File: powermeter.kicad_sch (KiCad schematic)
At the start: 21 parts, among them J1 Conn_01x04, J2 Conn_01x07, J3 Conn_01x07, Q1 S8550, U1 XIAO BLE, U2 HX711, U3 MPU-6050

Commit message: Fix 5v-GND short. Minor tweaks on layout
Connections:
- net GND: no longer J3.7 (Pin_7), U1.14 (5v)
- new net 5V: J3.7 (Pin_7), U1.14 (5v)

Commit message: Fix AD0 MPU6050 to GND
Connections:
- net GND: now also U3.9 (AD0)
- no-connect marks 6 -> 5
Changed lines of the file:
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@@
   (no_connect (at 88.9 91.44))
   (no_connect (at 220.98 59.69))
-  (no_connect (at 88.9 81.28))
   (no_connect (at 124.46 83.82))
   (wire (pts (xy 72.39 30.48) (xy 87.63 30.48))
@@
   )
   (wire (pts (xy 157.48 62.23) (xy 157.48 69.85))
+    (stroke (width 0) (type default))
+  )
+  (wire (pts (xy 86.36 81.28) (xy 88.9 81.28))
     (stroke (width 0) (type default))
   )
@@
         )
       )
+    )
+  )
+  (symbol (lib_id "power:GND") (at 86.36 81.28 270) (mirror x) (unit 1)
+    (in_bom yes) (on_board yes) (dnp no) (fields_autoplaced)
+    (property "Reference" "#PWR019" (at 80.01 81.28 0)
+      (effects (font (size 1.27 1.27)) hide)
+    )
+    (property "Value" "GND" (at 82.55 81.28 90)
+      (effects (font (size 1.27 1.27)) (justify right))
+    )
+    (property "Footprint" "" (at 86.36 81.28 0)
+      (effects (font (size 1.27 1.27)) hide)
+    )
+    (property "Datasheet" "" (at 86.36 81.28 0)
+      (effects (font (size 1.27 1.27)) hide)
+    )
+    (pin "1")
+    (instances
+      (project "powermeter"
+        (path "/59c6f472-5476-453e-ab78-e7815b2e4e17"
+          (reference "#PWR019") (unit 1)
+        )
+      )

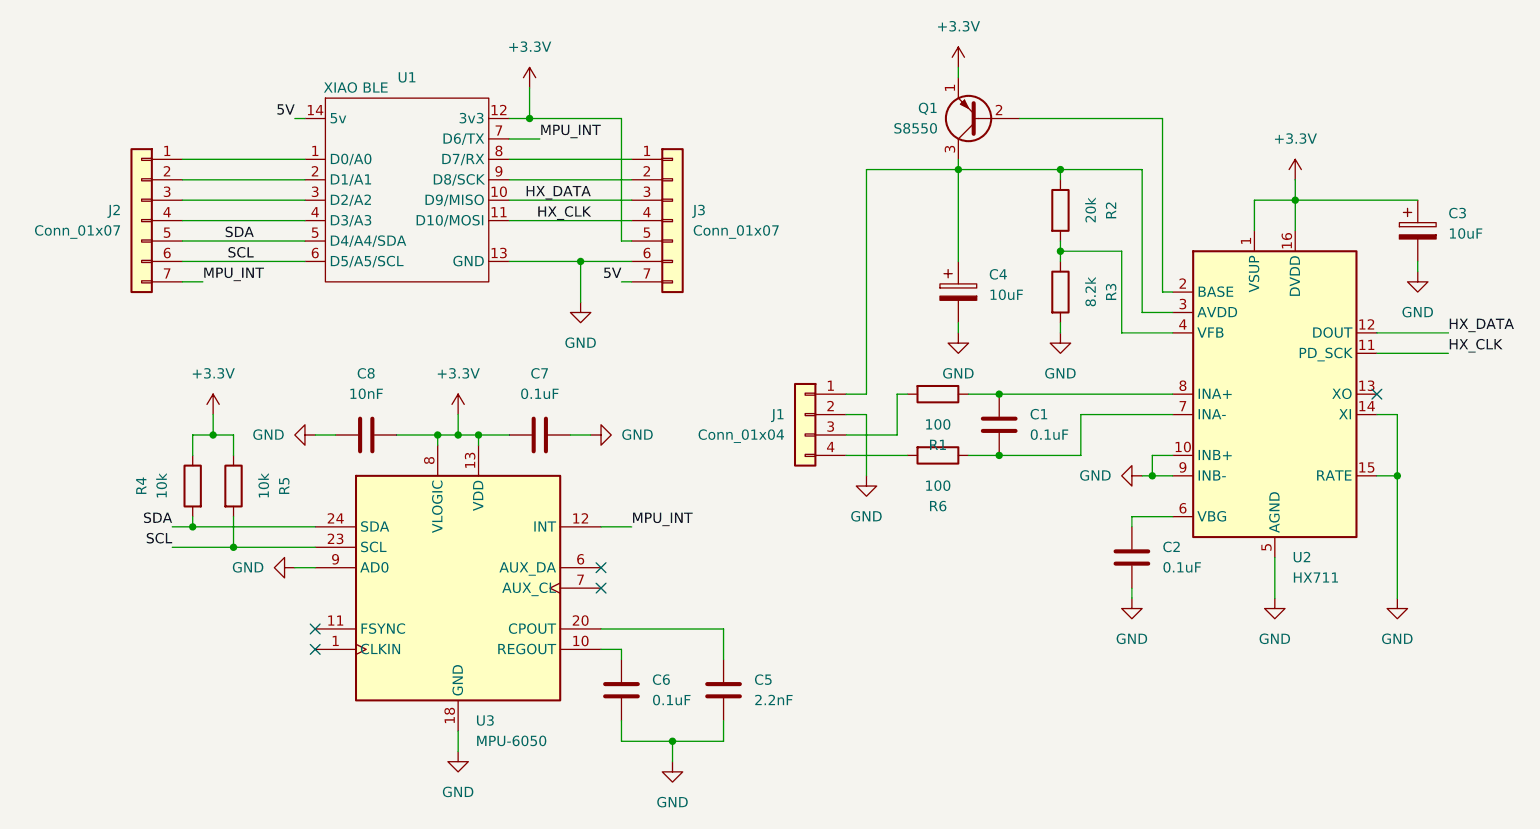
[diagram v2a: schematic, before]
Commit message: Change MPU6050 to LIS6DS3TRC
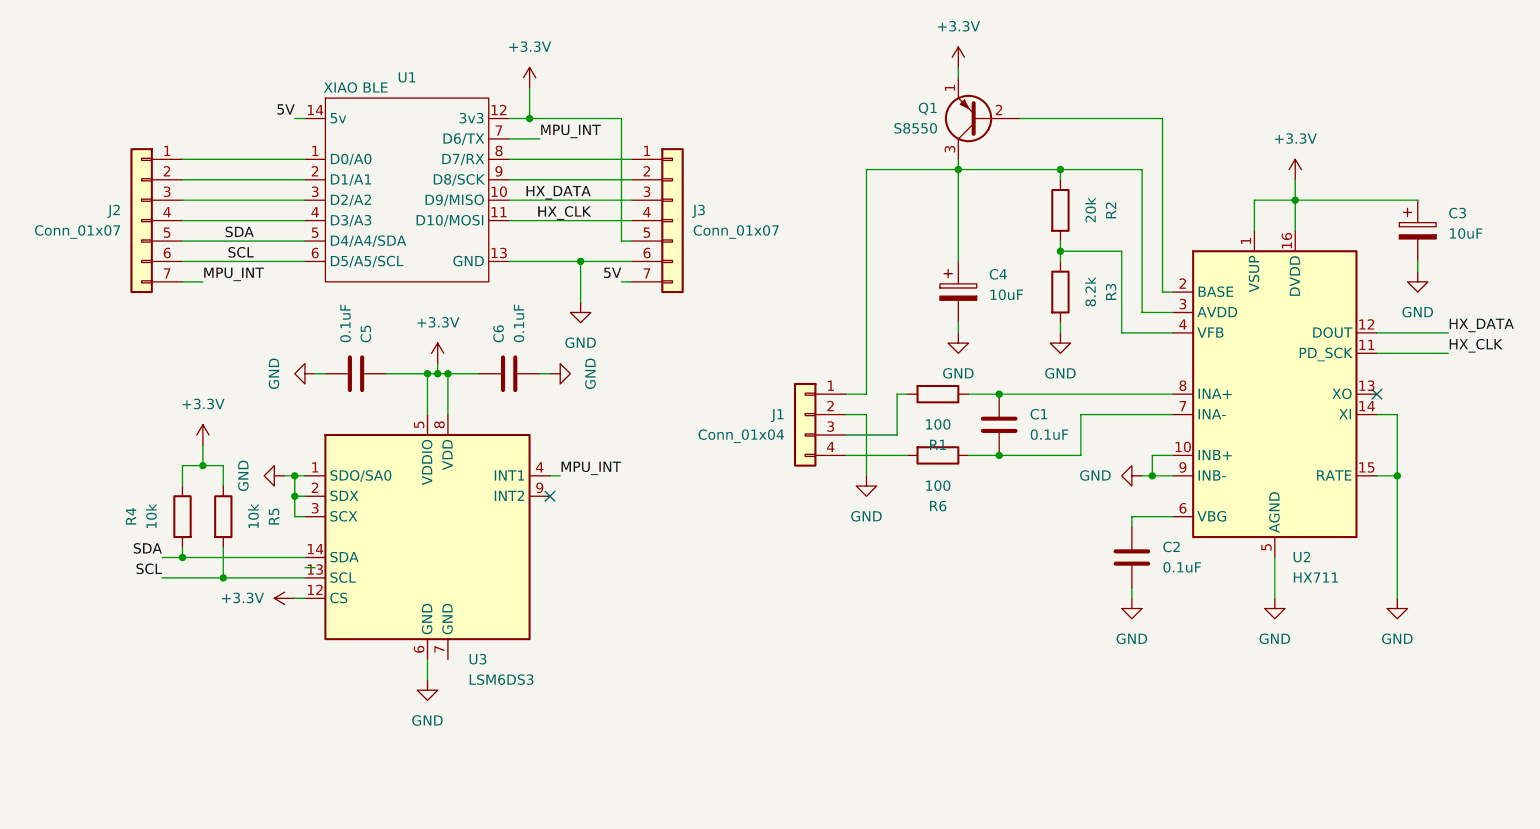
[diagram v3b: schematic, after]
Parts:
- removed C7: 0.1uF, Capacitor_SMD:C_0402_1005Metric, symbol Device:C
- removed C8: 10nF, Capacitor_SMD:C_0402_1005Metric, symbol Device:C
- removed U3: MPU-6050, Sensor_Motion:InvenSense_QFN-24_4x4mm_P0.5mm, symbol Sensor_Motion:MPU-6050
- added U3: LSM6DS3, Package_LGA:LGA-14_3x2.5mm_P0.5mm_LayoutBorder3x4y, symbol Sensor_Motion:LSM6DS3
- C5: value 2.2nF -> 0.1uF; LCSC C1604 -> C1525
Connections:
- net +3.3V: now also C5.2, C6.1, U3.12 (CS), U3.5 (VDDIO), U3.8 (VDD)
- net GND: now also C5.1, U3.1 (SDO/SA0), U3.2 (SDX), U3.3 (SCX), U3.6 (GND), U3.7 (GND); no longer C5.2
- net MPU_INT: now also U3.4 (INT1)
- net SCL: now also U3.13 (SCL)
- net SDA: now also U3.14 (SDA)
- no-connect marks 5 -> 2
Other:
- moved on the sheet: R4, R5
